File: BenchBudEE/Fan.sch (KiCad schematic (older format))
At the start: 9 parts, among them Q2 MOSFET_N, Q3 MOSFET_N, Q4 MOSFET_N, U10 MCP4922-E/P, U4 OPA4170

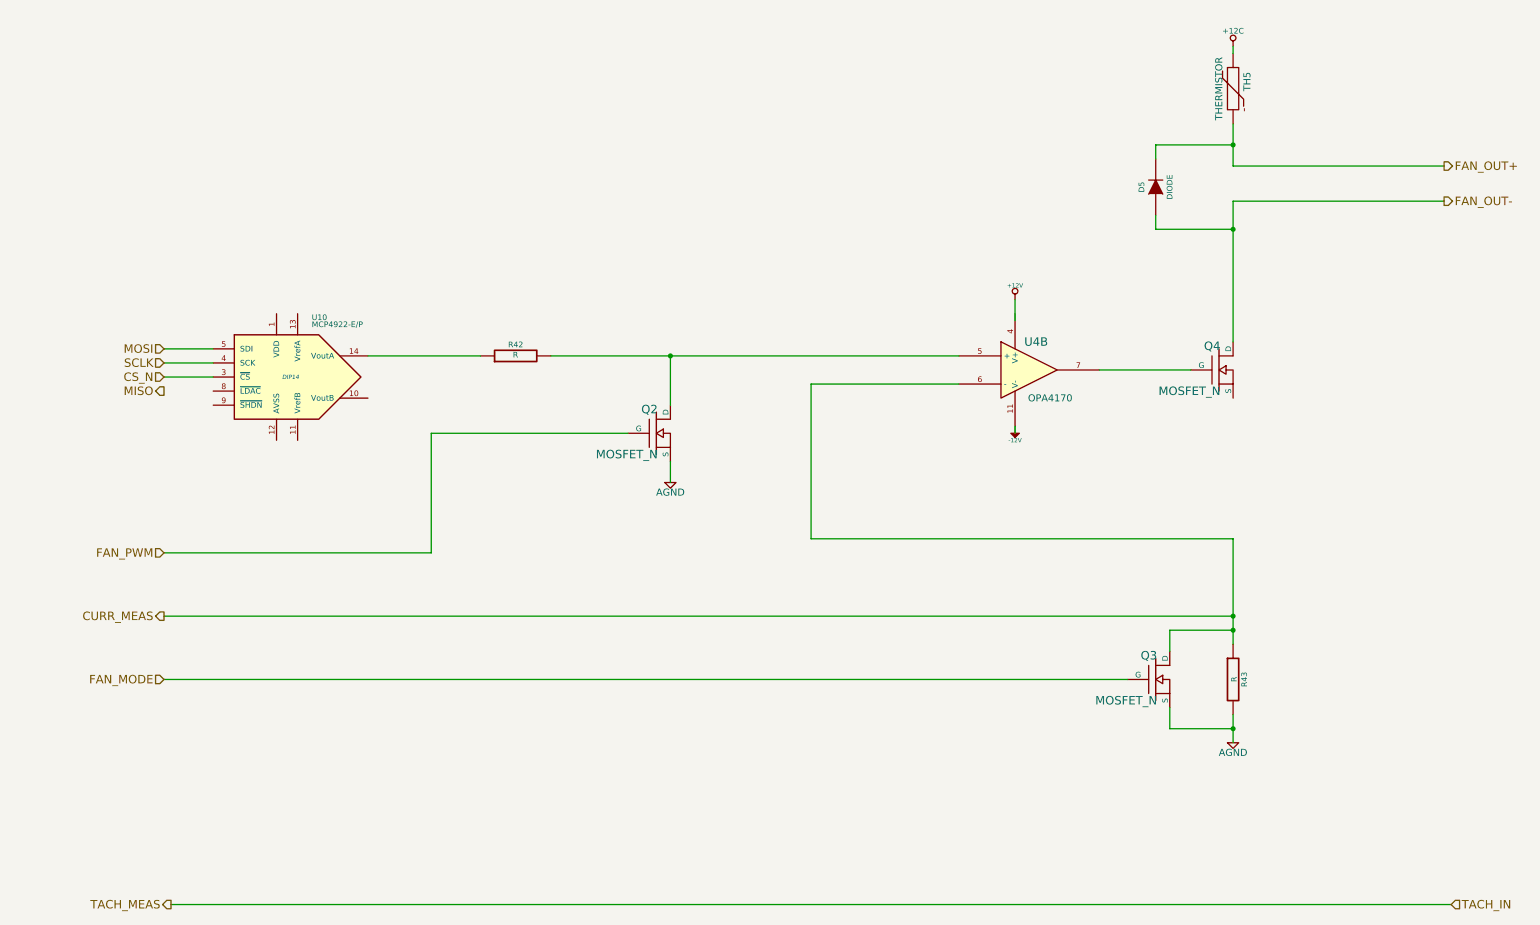
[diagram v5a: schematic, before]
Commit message: Associating and Placing Fan Module
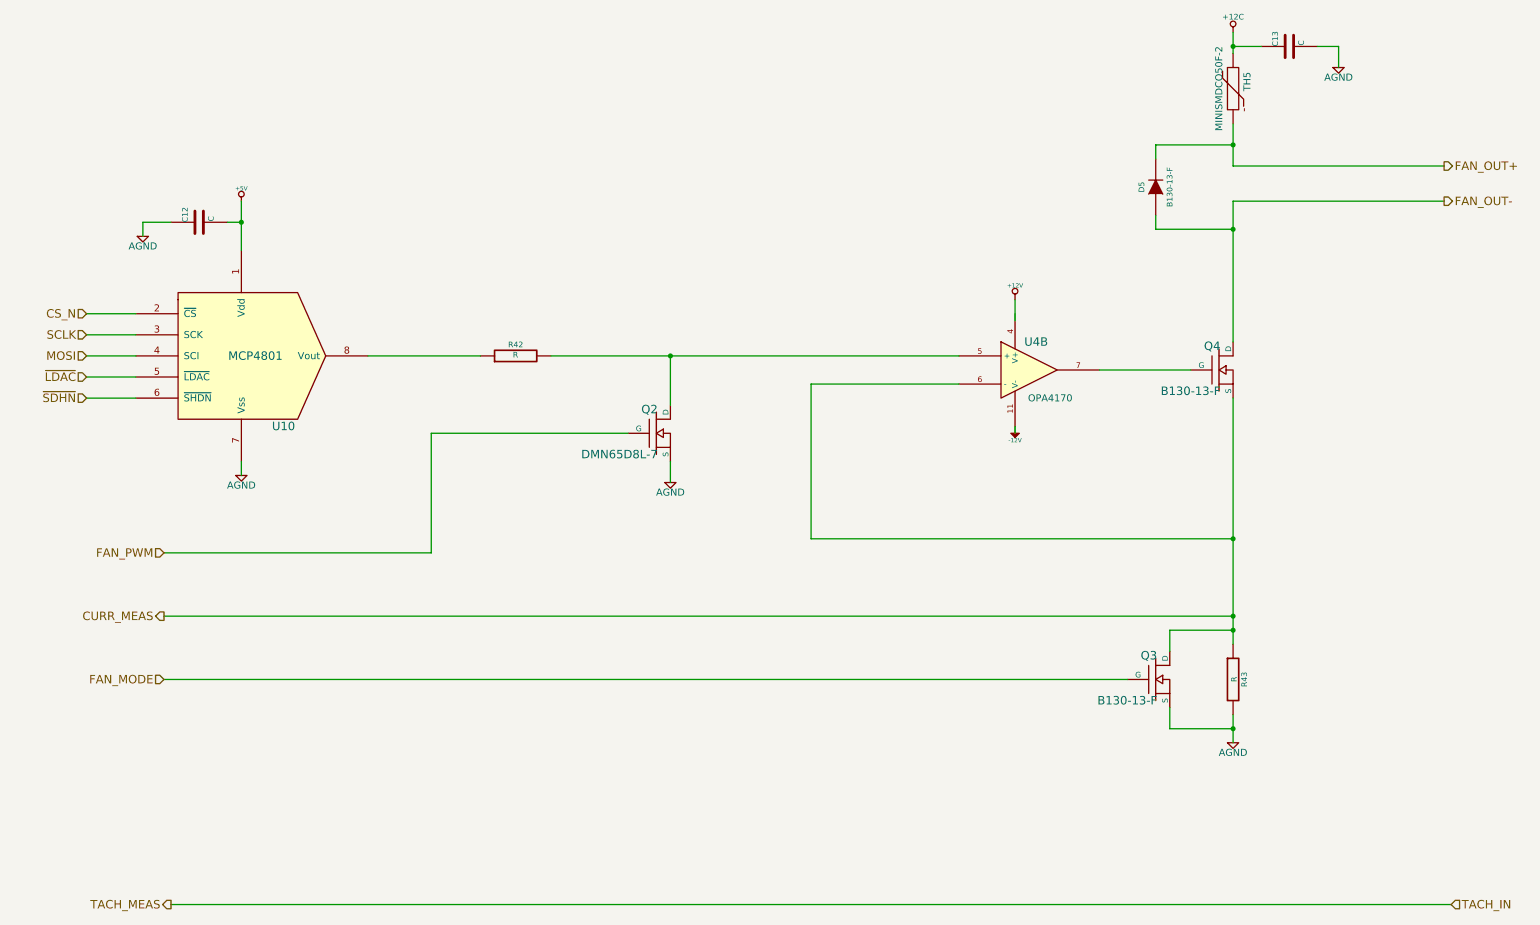
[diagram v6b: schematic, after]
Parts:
- removed Q3, Q4: MOSFET_N, ~, symbol MOSFET_N
- removed U10: MCP4922-E/P, DIP14, symbol MCP4922-E/P
- added C12, C13: C, ~, symbol C
- added Q3, Q4: B130-13-F, ~, symbol MOS_N_NUM
- added U10: MCP4801, symbol MCP4801
- D5: value DIODE -> B130-13-F; MFG Name (none) -> Diodes Inc; MFG Part Number (none) -> B130-13-F
- Q2: value MOSFET_N -> DMN65D8L-7; footprint ~ -> (none); MFG Name (none) -> Diodes Inc; MFG Part Number (none) -> DMN65D8L-7
- TH5: value THERMISTOR -> MINISMDCO50F-2; MFG Name (none) -> TE Connectivity; MFG Part Number (none) -> MINISMDCO50F-2
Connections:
- net labels added: +5V, ~LDAC, ~SDHN
- net labels removed: MISO
- wire segments 34 -> 44
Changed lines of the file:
@@
-	1    0    0    -1
-$EndComp
-$Comp
-L MOSFET_N Q4
-U 1 1 52F13D3A
-P 9000 3100
-F 0 "Q4" H 9010 3270 60  0000 R CNN
-F 1 "MOSFET_N" H 9010 2950 60  0000 R CNN
-F 2 "~" H 9000 3100 60  0000 C CNN
-F 3 "~" H 9000 3100 60  0000 C CNN
-	1    9000 3100
 	1    0    0    -1
 $EndComp
@@
 	8150 3100 8800 3100
 Wire Wire Line
-	9100 4300 9100 5050
+	9100 3300 9100 5050
 $Comp
 L R R43
@@
 $EndComp
 $Comp
-L AGND #PWR056
+L AGND #PWR66
 U 1 1 52F13D75
 P 9100 5750
-F 0 "#PWR056" H 9100 5750 40  0001 C CNN
+F 0 "#PWR66" H 9100 5750 40  0001 C CNN
 F 1 "AGND" H 9100 5680 50  0000 C CNN
 F 2 "" H 9100 5750 60  0000 C CNN
@@
 	6100 3200 7150 3200
 $Comp
-L +12V #PWR057
+L +12V #PWR63
 U 1 1 52F13D90
 P 7550 2600
-F 0 "#PWR057" H 7550 2550 20  0001 C CNN
+F 0 "#PWR63" H 7550 2550 20  0001 C CNN
 F 1 "+12V" H 7550 2700 30  0000 C CNN
 F 2 "" H 7550 2600 60  0000 C CNN
@@
 $EndComp
 $Comp
-L -12V #PWR058
+L -12V #PWR64
 U 1 1 52F13D98
 P 7550 3500
-F 0 "#PWR058" H 7550 3630 20  0001 C CNN
+F 0 "#PWR64" H 7550 3630 20  0001 C CNN
 F 1 "-12V" H 7550 3600 30  0000 C CNN
 F 2 "" H 7550 3500 60  0000 C CNN
@@
 	5100 3750 5100 3900
 $Comp
-L AGND #PWR059
+L AGND #PWR62
 U 1 1 52F13E8F
 P 5100 3900
-F 0 "#PWR059" H 5100 3900 40  0001 C CNN
+F 0 "#PWR62" H 5100 3900 40  0001 C CNN
 F 1 "AGND" H 5100 3830 50  0000 C CNN
 F 2 "" H 5100 3900 60  0000 C CNN
 F 3 "" H 5100 3900 60  0000 C CNN
 	1    5100 3900
-	1    0    0    -1
-$EndComp
-$Comp
-L MCP4922-E/P U10
-U 1 1 52F13EA6
-P 2400 3150
-F 0 "U10" H 2550 3550 40  0000 L BNN
-F 1 "MCP4922-E/P" H 2550 3500 40  0000 L BNN
-F 2 "DIP14" H 2400 3150 30  0000 C CIN
-F 3 "" H 2400 3150 60  0000 C CNN
-	1    2400 3150
 	1    0    0    -1
 $EndComp
@@
 Wire Wire Line
 	3750 3000 2950 3000
-Text HLabel 1500 2950 0    60   Input ~ 0
+Text HLabel 950  3000 0    60   Input ~ 0
 MOSI
-Text HLabel 1500 3250 0    60   Output ~ 0
-MISO
-Text HLabel 1500 3150 0    60   Input ~ 0
+Text HLabel 950  2700 0    60   Input ~ 0
 CS_N
-Text HLabel 1500 3050 0    60   Input ~ 0
+Text HLabel 950  2850 0    60   Input ~ 0
 SCLK
 Wire Wire Line
-	1500 2950 1850 2950
-Wire Wire Line
-	1500 3050 1850 3050
-Wire Wire Line
-	1500 3150 1850 3150
-$Comp
-L MOSFET_N Q3
-U 1 1 52FA6D72
-P 8550 5300
-F 0 "Q3" H 8560 5470 60  0000 R CNN
-F 1 "MOSFET_N" H 8560 5150 60  0000 R CNN
-F 2 "~" H 8550 5300 60  0000 C CNN
-F 3 "~" H 8550 5300 60  0000 C CNN
-	1    8550 5300
-	1    0    0    -1
-$EndComp
+	950  3000 1300 3000
+Wire Wire Line
+	950  2850 1300 2850
+Wire Wire Line
+	950  2700 1300 2700
 $Comp
 L THERMISTOR TH5
@@
 P 9100 1100
 F 0 "TH5" V 9200 1150 50  0000 C CNN
-F 1 "THERMISTOR" V 9000 1100 50  0000 C CNN
+F 1 "MINISMDCO50F-2" V 9000 1100 50  0000 C CNN
 F 2 "~" H 9100 1100 60  0000 C CNN
 F 3 "~" H 9100 1100 60  0000 C CNN
+F 4 "TE Connectivity" H 9100 1100 60  0001 C CNN "MFG Name"
+F 5 "MINISMDCO50F-2" H 9100 1100 60  0001 C CNN "MFG Part Number"
 	1    9100 1100
 	1    0    0    -1
 $EndComp
 Wire Wire Line
-	9100 800  9100 850
+	9100 700  9100 850
 Wire Wire Line
 	9100 1350 9100 1650
@@
 P 8550 1800
 F 0 "D5" H 8550 1900 40  0000 C CNN
-F 1 "DIODE" H 8550 1700 40  0000 C CNN
+F 1 "B130-13-F" H 8550 1700 40  0000 C CNN
 F 2 "~" H 8550 1800 60  0000 C CNN
 F 3 "~" H 8550 1800 60  0000 C CNN
+F 4 "Diodes Inc" H 8550 1800 60  0001 C CNN "MFG Name"
+F 5 "B130-13-F" H 8550 1800 60  0001 C CNN "MFG Part Number"
 	1    8550 1800
 	0    -1   -1   0
@@
 P 5000 3550
 F 0 "Q2" H 5010 3720 60  0000 R CNN
-F 1 "MOSFET_N" H 5010 3400 60  0000 R CNN
-F 2 "~" H 5000 3550 60  0000 C CNN
+F 1 "DMN65D8L-7" H 5010 3400 60  0000 R CNN
+F 2 "" H 5000 3550 60  0000 C CNN
 F 3 "~" H 5000 3550 60  0000 C CNN
+F 4 "Diodes Inc" H 5000 3550 60  0001 C CNN "MFG Name"
+F 5 "DMN65D8L-7" H 5000 3550 60  0001 C CNN "MFG Part Number"
 	1    5000 3550
 	1    0    0    -1
@@
 FAN_MODE
 $Comp
-L +12C #PWR060
+L +12C #PWR65
 U 1 1 52FA7706
-P 9100 800
-F 0 "#PWR060" H 9100 770 30  0001 C CNN
-F 1 "+12C" H 9100 910 40  0000 C CNN
-F 2 "" H 9100 800 60  0000 C CNN
-F 3 "" H 9100 800 60  0000 C CNN
-	1    9100 800
-	1    0    0    -1
-$EndComp
+P 9100 700
+F 0 "#PWR65" H 9100 670 30  0001 C CNN
+F 1 "+12C" H 9100 810 40  0000 C CNN
+F 2 "" H 9100 700 60  0000 C CNN
+F 3 "" H 9100 700 60  0000 C CNN
+	1    9100 700
+	1    0    0    -1
+$EndComp
+$Comp
+L MCP4801 U10
+U 1 1 5308CEB6
+P 2050 3000
+F 0 "U10" H 2350 2500 60  0000 C CNN
+F 1 "MCP4801" H 2150 3000 60  0000 C CNN
+F 2 "" H 2200 3400 60  0000 C CNN
+F 3 "" H 2200 3400 60  0000 C CNN
+	1    2050 3000
+	1    0    0    -1
+$EndComp
+Text HLabel 950  3150 0    60   Input ~ 0
+~LDAC
+Text HLabel 950  3300 0    60   Input ~ 0
+~SDHN
+Wire Wire Line
+	950  3150 1300 3150
+Wire Wire Line
+	1300 3300 950  3300
+$Comp
+L C C12
+U 1 1 5309268B
+P 1750 2050
+F 0 "C12" H 1750 2150 40  0000 L CNN
+F 1 "C" H 1756 1965 40  0000 L CNN
+F 2 "~" H 1788 1900 30  0000 C CNN
+F 3 "~" H 1750 2050 60  0000 C CNN
+	1    1750 2050
+	0    -1   -1   0
+$EndComp
+$Comp
+L +5V #PWR60
+U 1 1 53092691
+P 2050 1900
+F 0 "#PWR60" H 2050 1990 20  0001 C CNN
+F 1 "+5V" H 2050 1990 30  0000 C CNN
+F 2 "" H 2050 1900 60  0000 C CNN
+F 3 "" H 2050 1900 60  0000 C CNN
+	1    2050 1900
+	1    0    0    -1
+$EndComp
+$Comp
+L AGND #PWR59
+U 1 1 53092697
+P 1350 2150
+F 0 "#PWR59" H 1350 2150 40  0001 C CNN
+F 1 "AGND" H 1350 2080 50  0000 C CNN
+F 2 "" H 1350 2150 60  0000 C CNN
+F 3 "" H 1350 2150 60  0000 C CNN
+	1    1350 2150
+	1    0    0    -1
+$EndComp
+Wire Wire Line
+	2050 1900 2050 2250
+Wire Wire Line
+	2050 2050 1950 2050
+Connection ~ 2050 2050
+Wire Wire Line
+	1550 2050 1350 2050
+Wire Wire Line
+	1350 2050 1350 2150
+$Comp
+L AGND #PWR61
+U 1 1 530926A2
+P 2050 3850
+F 0 "#PWR61" H 2050 3850 40  0001 C CNN
+F 1 "AGND" H 2050 3780 50  0000 C CNN
+F 2 "" H 2050 3850 60  0000 C CNN
+F 3 "" H 2050 3850 60  0000 C CNN
+	1    2050 3850
+	1    0    0    -1
+$EndComp
+Wire Wire Line
+	2050 3750 2050 3850
+$Comp
+L C C13
+U 1 1 53092EED
+P 9500 800
+F 0 "C13" H 9500 900 40  0000 L CNN
+F 1 "C" H 9506 715 40  0000 L CNN
+F 2 "~" H 9538 650 30  0000 C CNN
+F 3 "~" H 9500 800 60  0000 C CNN
+	1    9500 800
+	0    -1   -1   0
+$EndComp
+Wire Wire Line
+	9100 800  9300 800
+Connection ~ 9100 800
+Wire Wire Line
+	9700 800  9850 800
+Wire Wire Line
+	9850 800  9850 950
+$Comp
+L AGND #PWR67
+U 1 1 53092F66
+P 9850 950
+F 0 "#PWR67" H 9850 950 40  0001 C CNN
+F 1 "AGND" H 9850 880 50  0000 C CNN
+F 2 "" H 9850 950 60  0000 C CNN
+F 3 "" H 9850 950 60  0000 C CNN
+	1    9850 950
+	1    0    0    -1
+$EndComp
+Connection ~ 9100 4300
+$Comp
+L MOS_N_NUM Q4
+U 1 1 53093330
+P 9000 3100
+F 0 "Q4" H 9010 3270 60  0000 R CNN
+F 1 "B130-13-F" H 9010 2950 60  0000 R CNN
+F 2 "~" H 9000 3100 60  0000 C CNN
+F 3 "~" H 9000 3100 60  0000 C CNN
+F 4 "Alpha and Omega" H 9000 3100 60  0001 C CNN "MFG Name"
+F 5 "B130-13-F" H 9000 3100 60  0001 C CNN "MFG Part Number"
+	1    9000 3100
+	1    0    0    -1
+$EndComp
+$Comp
+L MOS_N_NUM Q3
+U 1 1 53093393
+P 8550 5300
+F 0 "Q3" H 8560 5470 60  0000 R CNN
+F 1 "B130-13-F" H 8560 5150 60  0000 R CNN
+F 2 "~" H 8550 5300 60  0000 C CNN
+F 3 "~" H 8550 5300 60  0000 C CNN
+F 4 "Alpha and Omega" H 8550 5300 60  0001 C CNN "MFG Name"
+F 5 "B130-13-F" H 8550 5300 60  0001 C CNN "MFG Part Number"
+	1    8550 5300
+	1    0    0    -1
+$EndComp
